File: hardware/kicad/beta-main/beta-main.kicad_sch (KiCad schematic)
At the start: 2 parts, among them J8 Conn_01x02_Socket, U1 MAX98357A

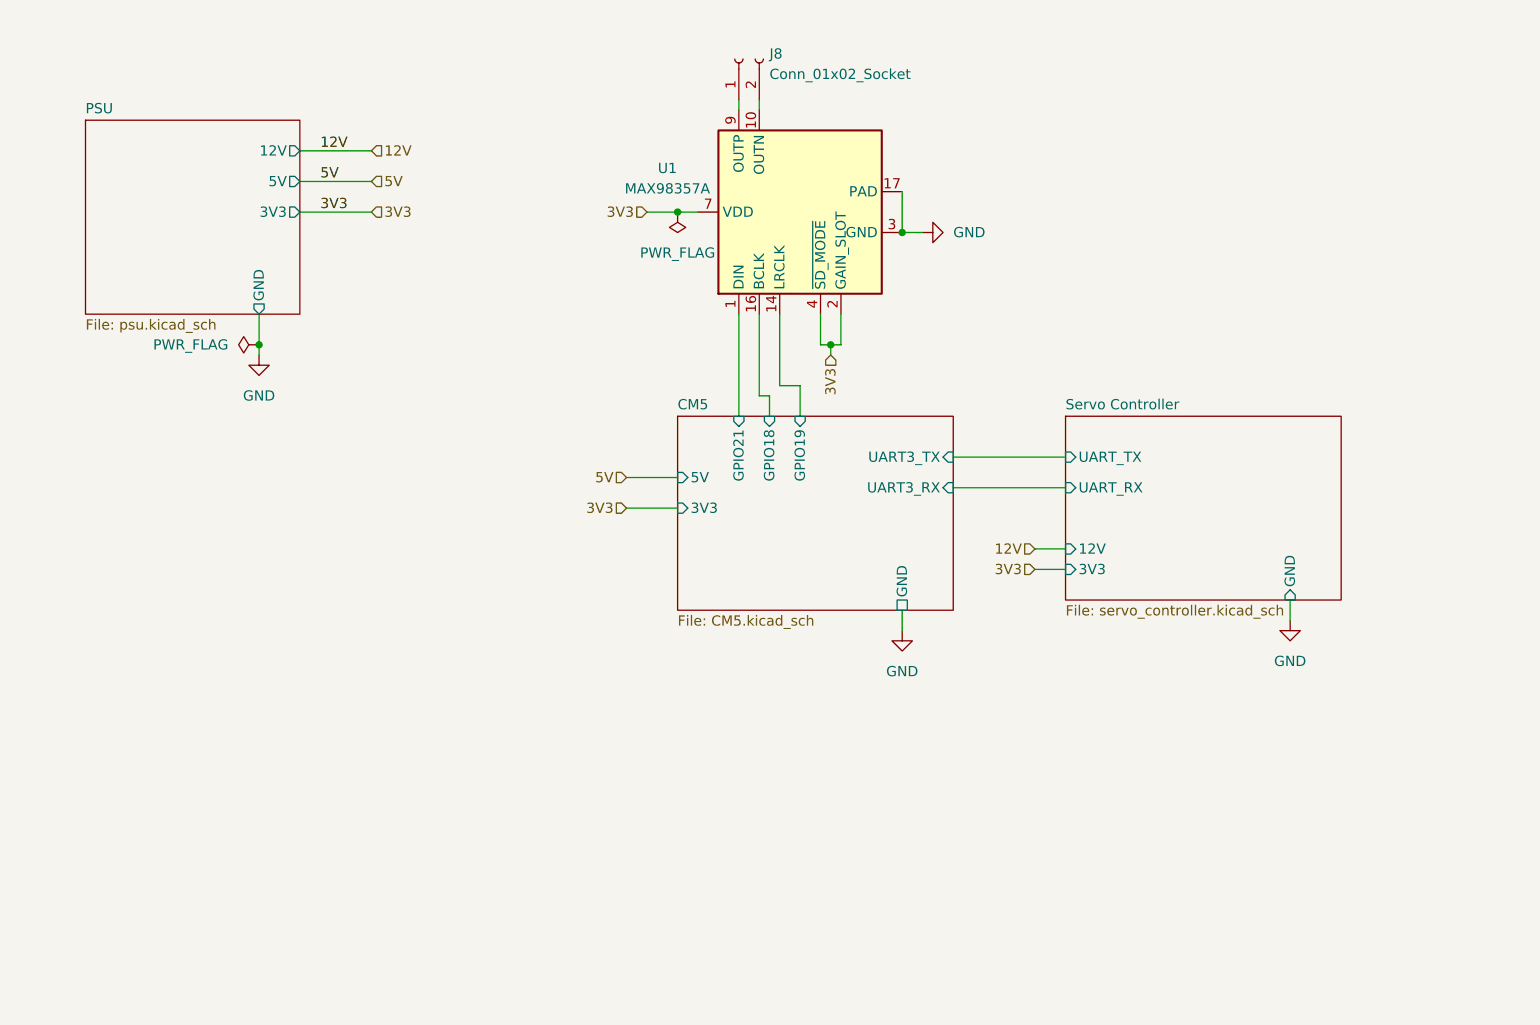
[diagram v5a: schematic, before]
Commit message: Gyroscope added without errors in ERC
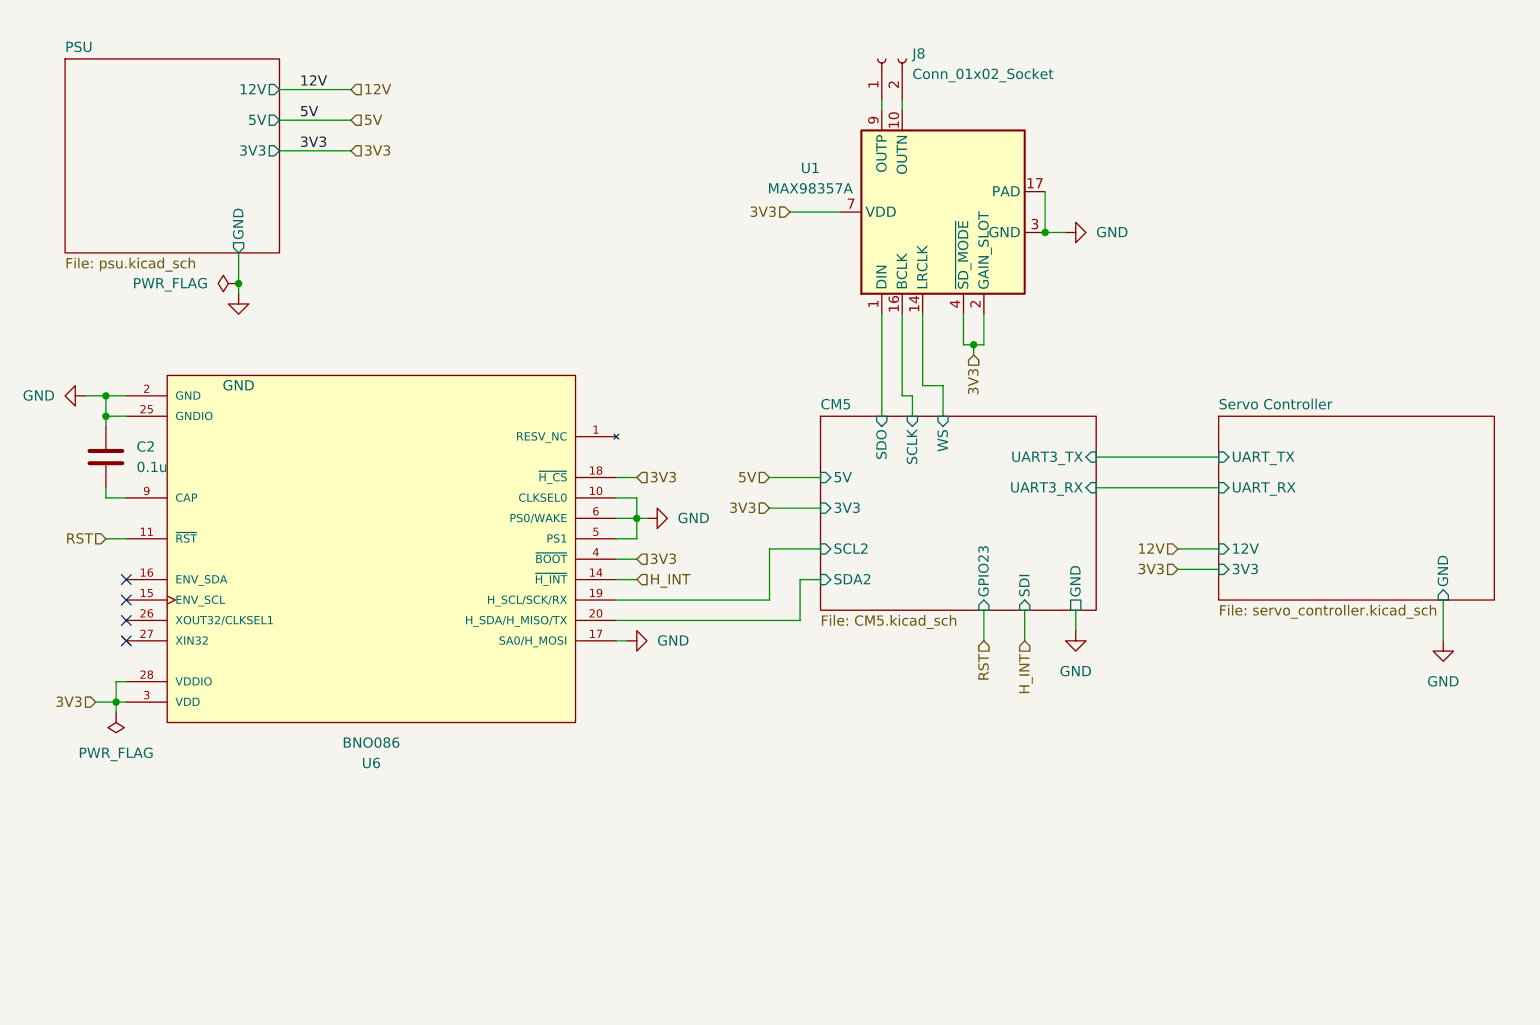
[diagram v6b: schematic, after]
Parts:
- added C2: 0.1u, symbol Device:C
- added U6: BNO086, BNO086:IC_BNO086, symbol BNO086:BNO086
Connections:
- net 3V3: now also U6.18 (~{H_CS}), U6.28 (VDDIO), U6.3 (VDD), U6.4 (~{BOOT})
- net GND: now also C2.1, U6.10 (CLKSEL0), U6.17 (SA0/H_MOSI), U6.2 (GND), U6.25 (GNDIO), U6.5 (PS1), U6.6 (PS0/WAKE)
- net CM5/GPIO18 renamed CM5/SCLK
- net CM5/GPIO19 renamed CM5/WS
- net CM5/GPIO21 renamed CM5/SDO
- new net: U6.1 (RESV_NC), U6.12 (RESV_NC), U6.13 (RESV_NC), U6.21 (RESV_NC), U6.22 (RESV_NC), U6.23 (RESV_NC), U6.24 (RESV_NC), U6.7 (RESV_NC), U6.8 (RESV_NC)
- new net: C2.2, U6.9 (CAP)
- new net CM5/SCL2: U6.19 (H_SCL/SCK/RX)
- new net CM5/SDA2: U6.20 (H_SDA/H_MISO/TX)
- new net H_INT: U6.14 (~{H_INT})
- new net RST: U6.11 (~{RST})
- no-connect marks 0 -> 4
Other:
- sheet CM5 ports: added GPIO23, SCL2, SCLK, SDA2, SDI, SDO, WS; removed GPIO18, GPIO19, GPIO21
- moved on the sheet: J8, U1

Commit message: Setup for PCB layout
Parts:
- added FID1, FID2, FID3: ~, Fiducial:Fiducial_1mm_Mask2mm, symbol Mechanical:Fiducial
- added MH1, MH2, MH3, MH4: M3, MountingHole:MountingHole_3.2mm_M3_Pad_Via, symbol Mechanical:MountingHole_Pad
- C2: footprint (none) -> Capacitor_SMD:C_0402_1005Metric
- J8: footprint (none) -> Connector_PinHeader_2.54mm:PinHeader_1x02_P2.54mm_Vertical
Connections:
- net GND: now also MH1.1, MH2.1, MH3.1, MH4.1

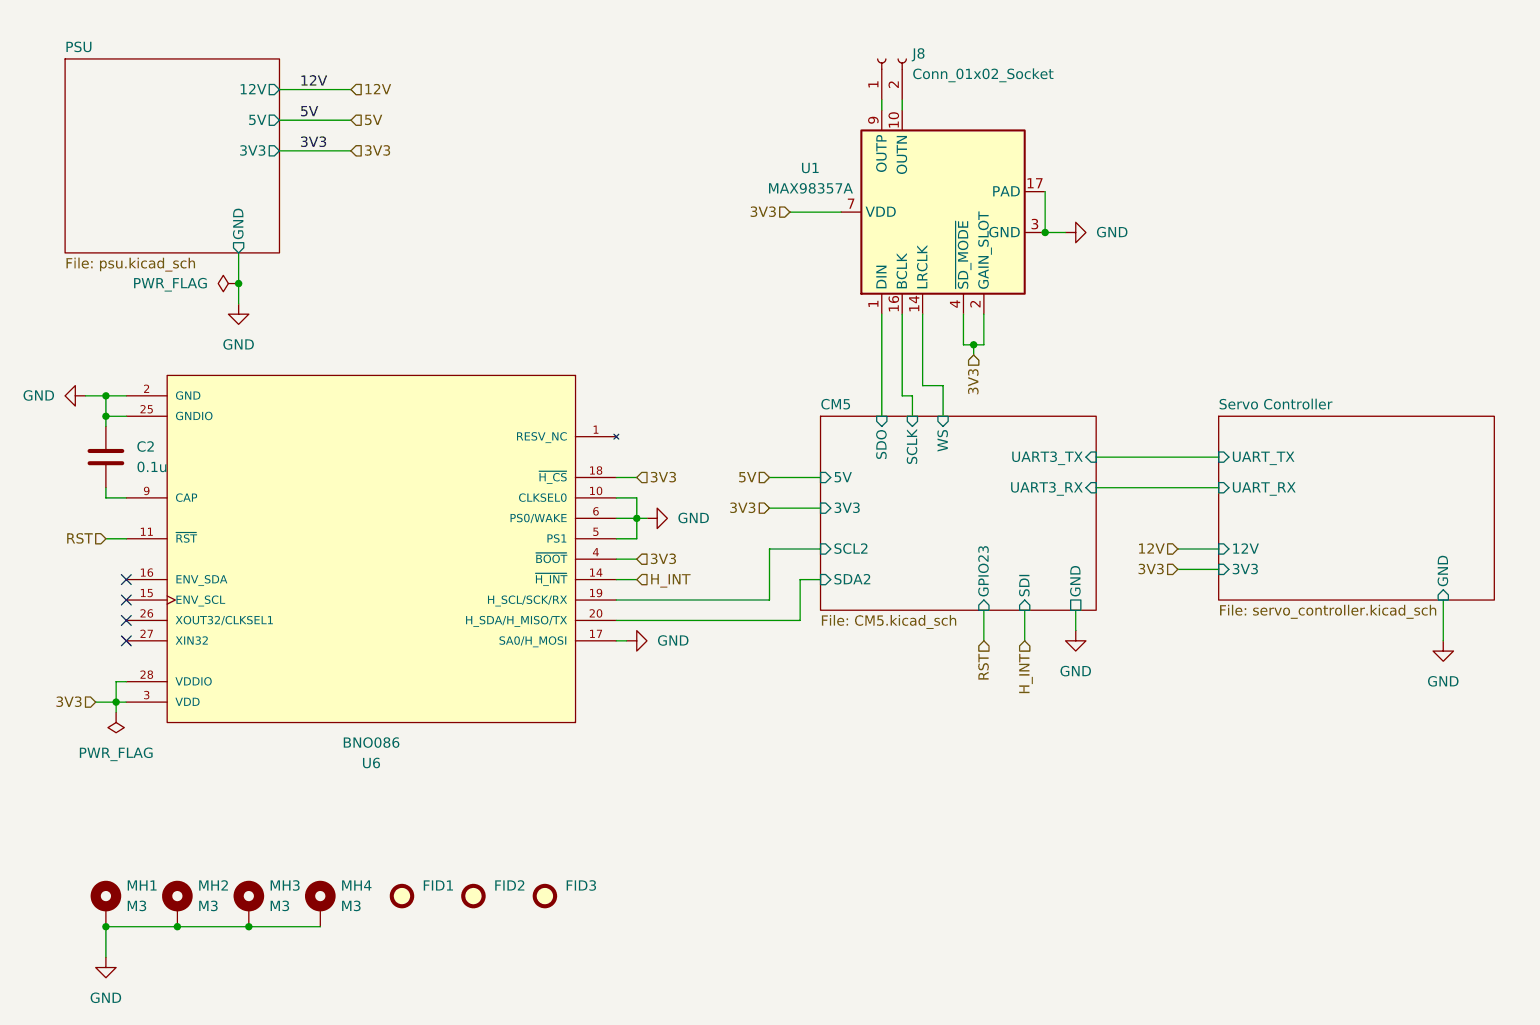
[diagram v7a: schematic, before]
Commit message: remove power symbols from hierarchy and move different subsystems  around
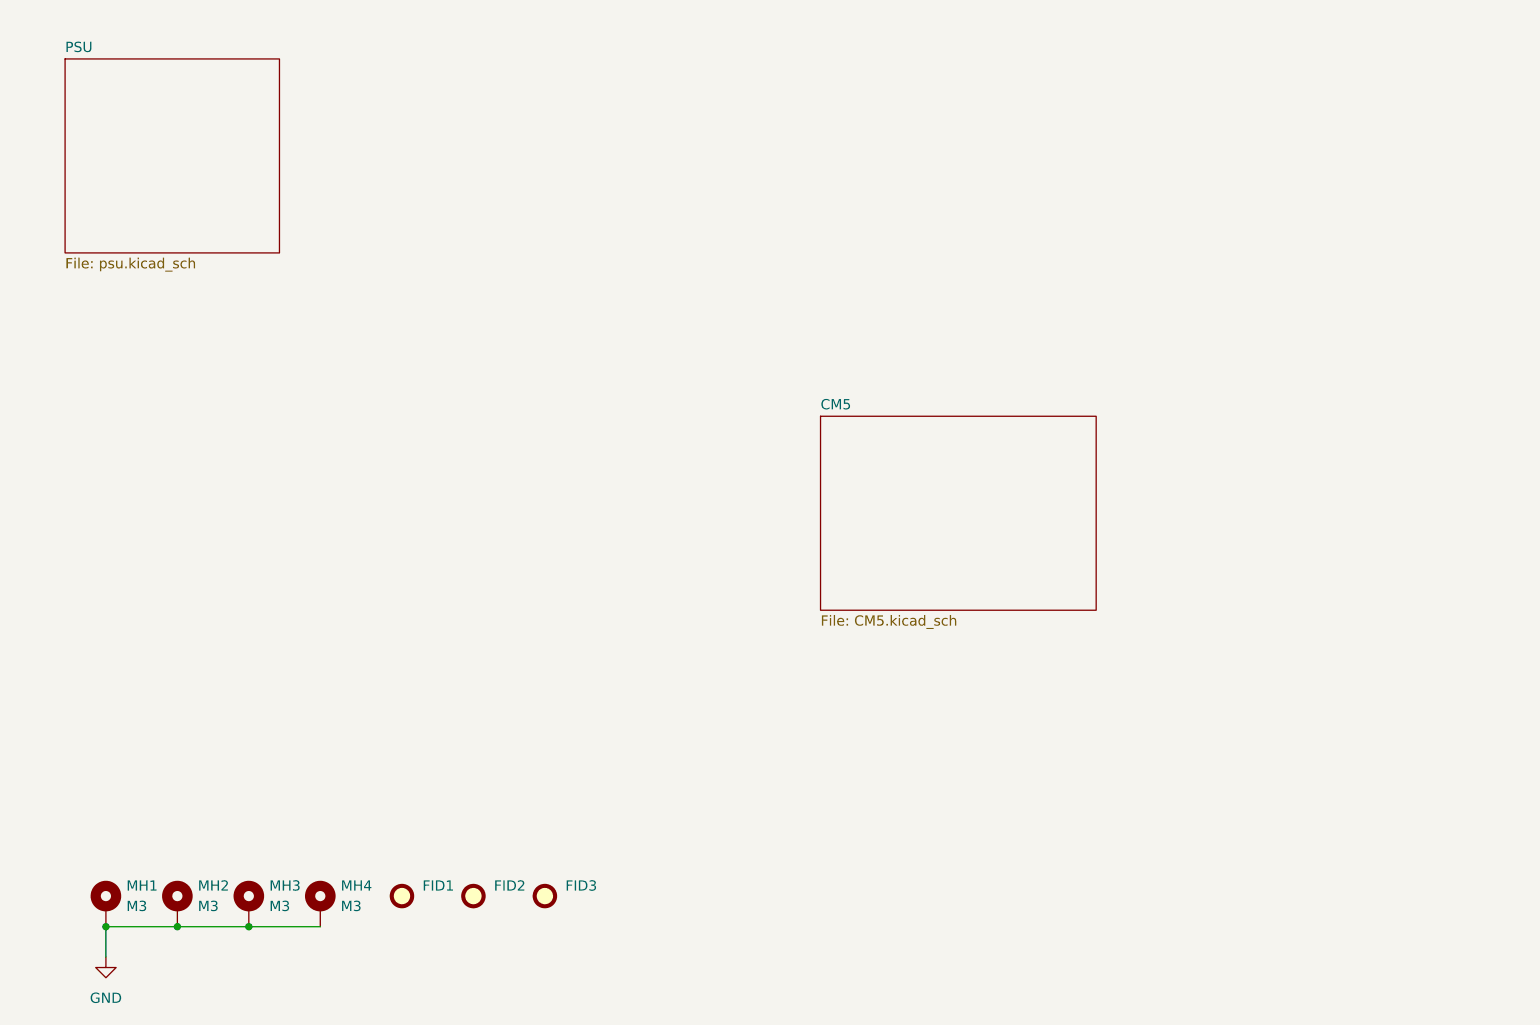
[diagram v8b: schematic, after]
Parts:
- removed C2: 0.1u, Capacitor_SMD:C_0402_1005Metric, symbol Device:C
- removed J8: Conn_01x02_Socket, Connector_PinHeader_2.54mm:PinHeader_1x02_P2.54mm_Vertical, symbol Connector:Conn_01x02_Socket
- removed U1: MAX98357A, Package_DFN_QFN:TQFN-16-1EP_3x3mm_P0.5mm_EP1.23x1.23mm, symbol Audio:MAX98357A
- removed U6: BNO086, BNO086:IC_BNO086, symbol BNO086:BNO086
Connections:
- no-connect marks 4 -> 0
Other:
- removed sheet Servo Controller
- sheet CM5 ports: added none; removed 3V3, 5V, GND, GPIO23, SCL2, SCLK, SDA2, SDI, SDO, UART3_RX, UART3_TX, WS
- sheet PSU ports: added none; removed 12V, 3V3, 5V, GND
